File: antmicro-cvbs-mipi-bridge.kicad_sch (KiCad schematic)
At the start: 105 parts, among them IC1 ADV7280BCPZ-M, IC2 TLV70018, IC4 SN74AUP1G17DCKR, IC5 SN74AUP1G17DCKR, J1 WE_68715014522, J2 61300211121, J7 61300211121, Q1 BSS138APW, Q2 BSS138APW, Q3 BSS138APW, Q4 BSS138APW, Y1 ABM8G-28.63636MHZ-18-D2Y-T

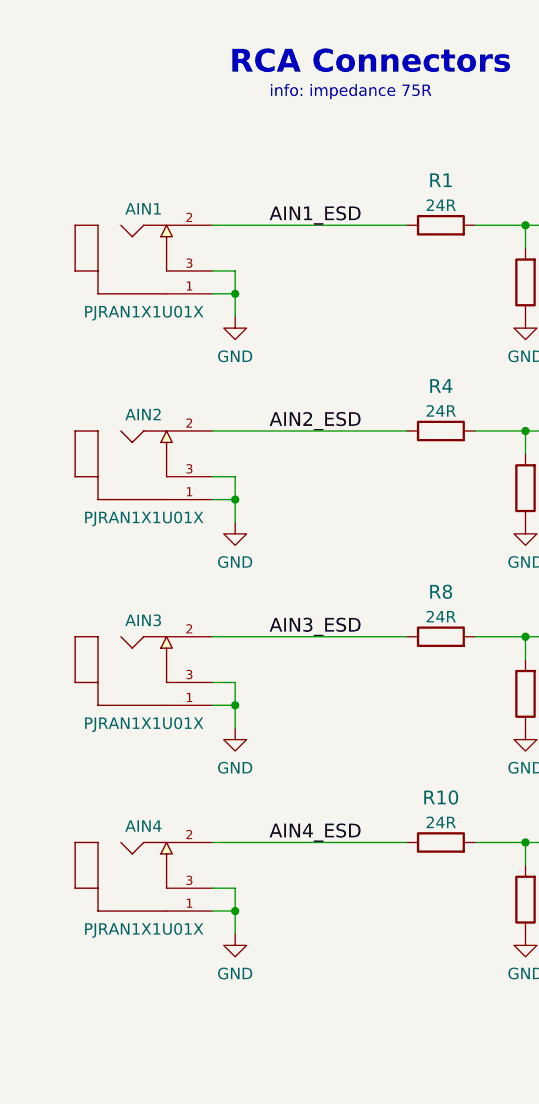
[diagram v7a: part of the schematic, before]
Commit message: loclib. Added new components from schematic after review
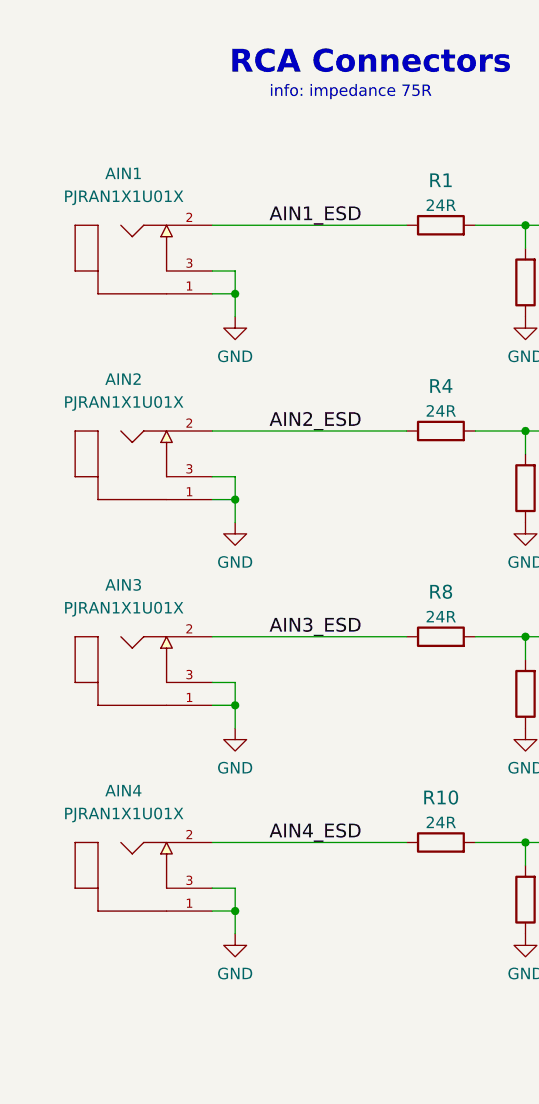
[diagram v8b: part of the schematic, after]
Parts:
- removed AIN1, AIN2, AIN3, AIN4: PJRAN1X1U01X, antmicro-footprints:PJRAN1X1U01X, symbol antmicroRCAConnectors:PJRAN1X1U01X
- added AIN1, AIN2, AIN3, AIN4: PJRAN1X1U01X, antmicro-cvbs-mipi-bridge-footprints:PJRAN1X1U01X, symbol antmicro-cvbs-mipi-bridge:PJRAN1X1U01X
- AGPO0, AGPO1, D5, D6: footprint antmicro-footprints:LED_0603 -> antmicro-cvbs-mipi-bridge-footprints:LED_0603; symbol antmicroLEDIndicationDiscrete:KP-1608ZGC -> antmicro-cvbs-mipi-bridge:KP-1608ZGC
- C1, C10, C13, C14, C16, C17, C2, C20, C21, C24, C26, C3, C4, C5, C6, C7: footprint antmicro-footprints:0402-cap -> antmicro-cvbs-mipi-bridge-footprints:0402-cap; symbol antmicroCapacitors0402:C_100n_0402 -> antmicro-cvbs-mipi-bridge:C_100n_0402
- C11, C15, C18, C19: footprint antmicro-footprints:0402-cap -> antmicro-cvbs-mipi-bridge-footprints:0402-cap; symbol antmicroCapacitors0402:C_10n_0402 -> antmicro-cvbs-mipi-bridge:C_10n_0402
- C12: footprint antmicro-footprints:0603-cap -> antmicro-cvbs-mipi-bridge-footprints:0603-cap; symbol antmicro-jetson-agx-csi-adapter:C_1u_0603 -> antmicro-cvbs-mipi-bridge:C_1u_0603
- C22, C23: footprint antmicro-footprints:0402-cap -> antmicro-cvbs-mipi-bridge-footprints:0402-cap; symbol antmicroCapacitors0402:C_10p_0402 -> antmicro-cvbs-mipi-bridge:C_10p_0402
- C27, C28, C8, C9: footprint antmicro-footprints:0402-cap -> antmicro-cvbs-mipi-bridge-footprints:0402-cap; symbol antmicroCapacitors0402:C_1u_0402 -> antmicro-cvbs-mipi-bridge:C_1u_0402
- D1, D2, D3, D4: footprint antmicro-footprints:SOT-23-3 -> antmicro-cvbs-mipi-bridge-footprints:SOT-23-3; symbol antmicroTVSDiodes:PESD1CAN_215 -> antmicro-cvbs-mipi-bridge:PESD1CAN_215
- FB1, FB3, FB4, FB5: footprint antmicro-footprints:0805-res -> antmicro-cvbs-mipi-bridge-footprints:0805-res; symbol antmicroFerriteBeadsandChips:742792022 -> antmicro-cvbs-mipi-bridge:742792022
- IC1: footprint antmicro-footprints:LFCSP-32-1EP-5x5mm -> antmicro-cvbs-mipi-bridge-footprints:LFCSP-32-1EP-5x5mm; symbol antmicroDataAcquisitionAnalogtoDigitalConvertersADC:ADV7280BCPZ-M -> antmicro-cvbs-mipi-bridge:ADV7280BCPZ-M
- IC2: footprint antmicro-footprints:SC-70-5 -> antmicro-cvbs-mipi-bridge-footprints:SC-70-5; symbol antmicroPMICVoltageRegulatorsLinear:TLV70018 -> antmicro-cvbs-mipi-bridge:TLV70018
- IC4, IC5: footprint antmicro-footprints:SOT-753 -> antmicro-cvbs-mipi-bridge-footprints:SOT-753; symbol antmicroLogicBuffersDriversReceiversTransceivers:SN74AUP1G17DCKR -> antmicro-cvbs-mipi-bridge:SN74AUP1G17DCKR
- J1: footprint antmicro-footprints:WE_68715014522 -> antmicro-cvbs-mipi-bridge-footprints:WE_68715014522; symbol antmicroFCCConnectors:WE_68715014522 -> antmicro-cvbs-mipi-bridge:WE_68715014522
- J2, J7: footprint antmicro-footprints:PinHeader_1x2_P2.54_Drill0.9mm -> antmicro-cvbs-mipi-bridge-footprints:PinHeader_1x2_P2.54_Drill0.9mm; symbol antmicroRectangularConnectorsHeadersMalePins:61300211121 -> antmicro-cvbs-mipi-bridge:61300211121
- MP1, MP2, MP3, MP4: footprint antmicro-footprints:9774030243R -> antmicro-cvbs-mipi-bridge-footprints:9774030243R; symbol antmicroMechanicalParts:9774030243R -> antmicro-cvbs-mipi-bridge:9774030243R
- N1: footprint antmicro-footprints:antmicro-logo_scaled_20mm -> antmicro-cvbs-mipi-bridge-footprints:antmicro-logo_scaled_20mm; symbol antmicroMechanicalParts:antmicro_logo -> antmicro-cvbs-mipi-bridge:antmicro_logo
- N2: footprint antmicro-footprints:oshw-logo -> antmicro-cvbs-mipi-bridge-footprints:oshw-logo; symbol antmicroMechanicalParts:oshw_logo -> antmicro-cvbs-mipi-bridge:oshw_logo
- Q1, Q2, Q3, Q4: footprint antmicro-footprints:SC70-3 -> antmicro-cvbs-mipi-bridge-footprints:SC70-3; symbol antmicroTransistorsFETsMOSFETsSingle:BSS138APW -> antmicro-cvbs-mipi-bridge:BSS138APW
- R1, R10, R4, R8: footprint antmicro-footprints:0603-res -> antmicro-cvbs-mipi-bridge-footprints:0603-res; symbol antmicroResistors0603:R_24R_0603 -> antmicro-cvbs-mipi-bridge:R_24R_0603
- R11, R3, R5, R9: footprint antmicro-footprints:0402-res -> antmicro-cvbs-mipi-bridge-footprints:0402-res; symbol antmicroResistors0402:R_51R_0402 -> antmicro-cvbs-mipi-bridge:R_51R_0402
- R12, R13, R14, R26: footprint antmicro-footprints:0402-res -> antmicro-cvbs-mipi-bridge-footprints:0402-res; symbol antmicro-jetson-agx-csi-adapter:R_470R_0402 -> antmicro-cvbs-mipi-bridge:R_470R_0402
- R15: footprint antmicro-footprints:0402-res -> antmicro-cvbs-mipi-bridge-footprints:0402-res; symbol antmicroResistors0402:R_22k_0402 -> antmicro-cvbs-mipi-bridge:R_22k_0402
- R16: footprint antmicro-footprints:0402-res -> antmicro-cvbs-mipi-bridge-footprints:0402-res; symbol antmicroResistors0402:R_1M0_0402 -> antmicro-cvbs-mipi-bridge:R_1M0_0402
- R17, R18, R19, R27, R28, R29, R31: footprint antmicro-footprints:0402-res -> antmicro-cvbs-mipi-bridge-footprints:0402-res; symbol antmicroResistors0402:R_100k_0402 -> antmicro-cvbs-mipi-bridge:R_100k_0402
- R2: footprint antmicro-footprints:0402-res -> antmicro-cvbs-mipi-bridge-footprints:0402-res; symbol antmicroResistors0402:R_1k_0402 -> antmicro-cvbs-mipi-bridge:R_1k_0402
- R20, R21, R22, R23, R24, R25, R30: footprint antmicro-footprints:0402-res -> antmicro-cvbs-mipi-bridge-footprints:0402-res; symbol antmicroResistors0402:R_0R_0402 -> antmicro-cvbs-mipi-bridge:R_0R_0402
- R6, R7: footprint antmicro-footprints:0402-res -> antmicro-cvbs-mipi-bridge-footprints:0402-res; symbol antmicroResistors0402:R_4k7_0402 -> antmicro-cvbs-mipi-bridge:R_4k7_0402
- S1: footprint antmicro-footprints:SW_SPST_4.2x2.8 -> antmicro-cvbs-mipi-bridge-footprints:SW_SPST_4.2x2.8; symbol antmicroPushbuttonSwitches:KMR2 -> antmicro-cvbs-mipi-bridge:KMR2
- TP1, TP10, TP11, TP12, TP13, TP2, TP3, TP5, TP6, TP7, TP8, TP9: footprint antmicro-footprints:TP-R-1.5 -> antmicro-cvbs-mipi-bridge-footprints:TP-R-1.5; symbol antmicroTestPoints:TP -> antmicro-cvbs-mipi-bridge:TP
- Y1: footprint antmicro-footprints:KX-7 -> antmicro-cvbs-mipi-bridge-footprints:KX-7; symbol antmicroCrystals:ABM8G-28.63636MHZ-18-D2Y-T -> antmicro-cvbs-mipi-bridge:ABM8G-28.63636MHZ-18-D2Y-T
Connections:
- net AIN1_ESD: now also AIN1.2
- net AIN2_ESD: now also AIN2.2
- net AIN3_ESD: now also AIN3.2
- net AIN4_ESD: now also AIN4.2
- net GND: now also AIN1.1, AIN1.3, AIN2.1, AIN2.3, AIN3.1, AIN3.3, AIN4.1, AIN4.3
